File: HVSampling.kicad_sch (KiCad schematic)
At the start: 11 parts, among them K5 SPU01M-05, U13 TLV6002, U7 LM393, U8 4N35

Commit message: schematic: Assign all footprints
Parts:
- K5: footprint (none) -> yfs:DPU01M05
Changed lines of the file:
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@@
 			)
 		)
-		(property "Footprint" ""
+		(property "Footprint" "yfs:DPU01M05"
 			(at 177.8 35.56 0)
 			(effects

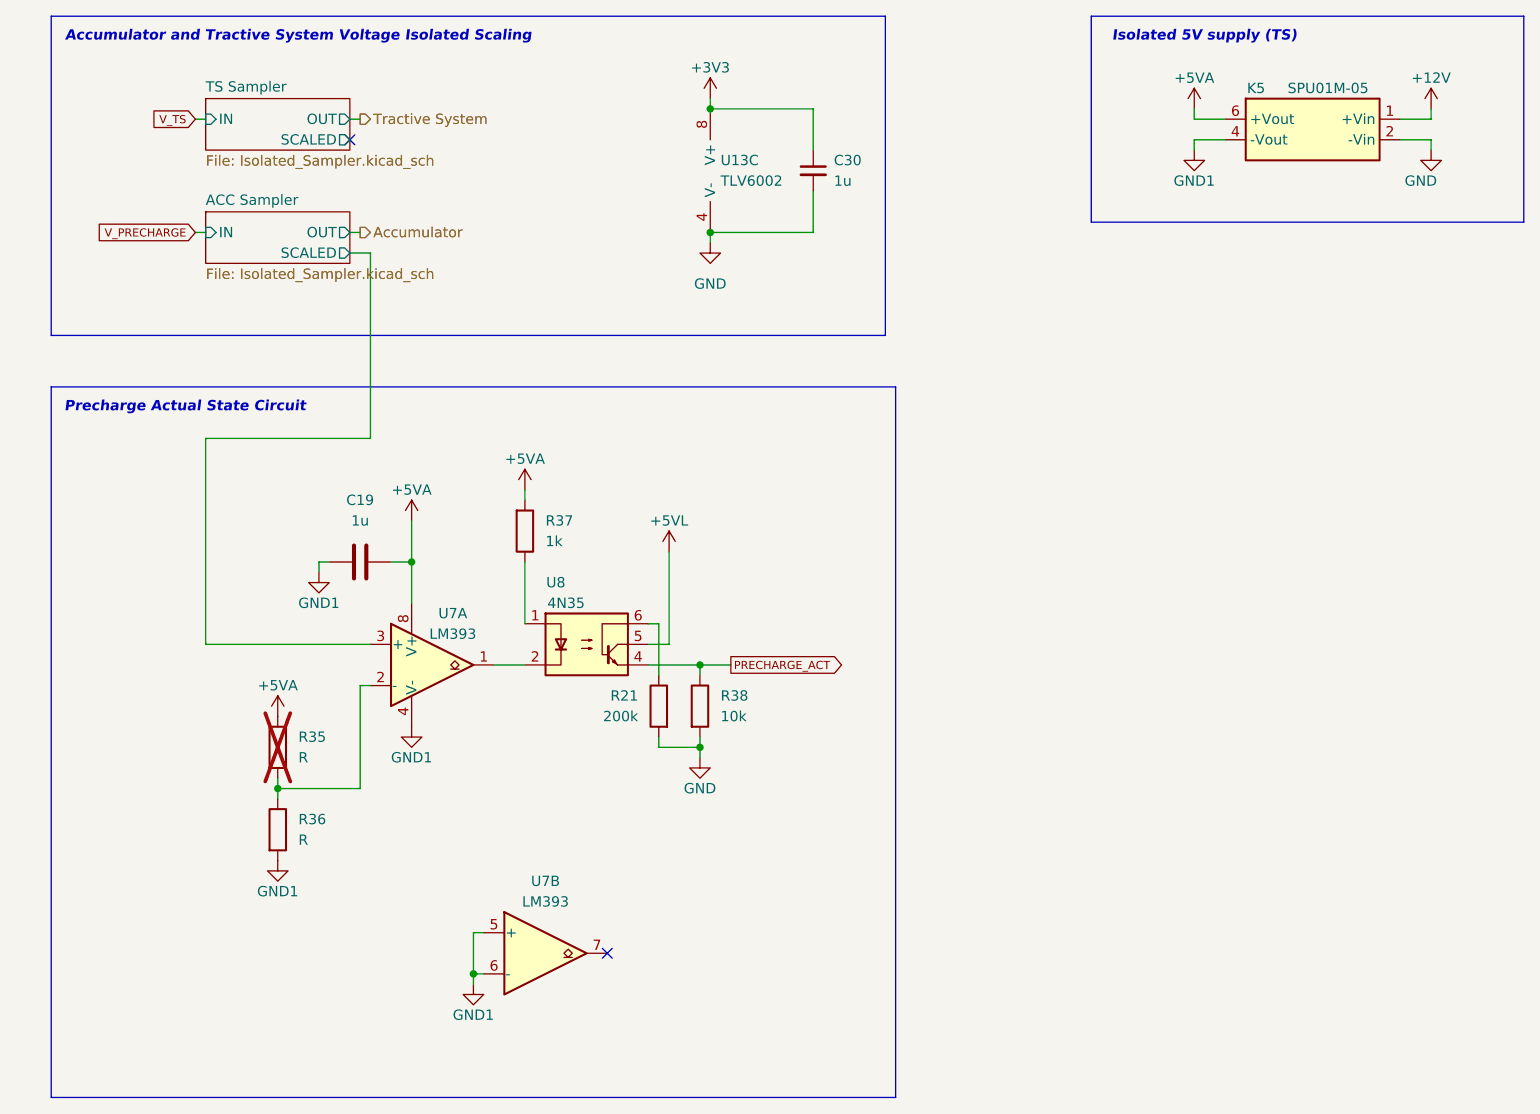
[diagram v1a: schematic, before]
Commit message: schematic: Reassign reference designators
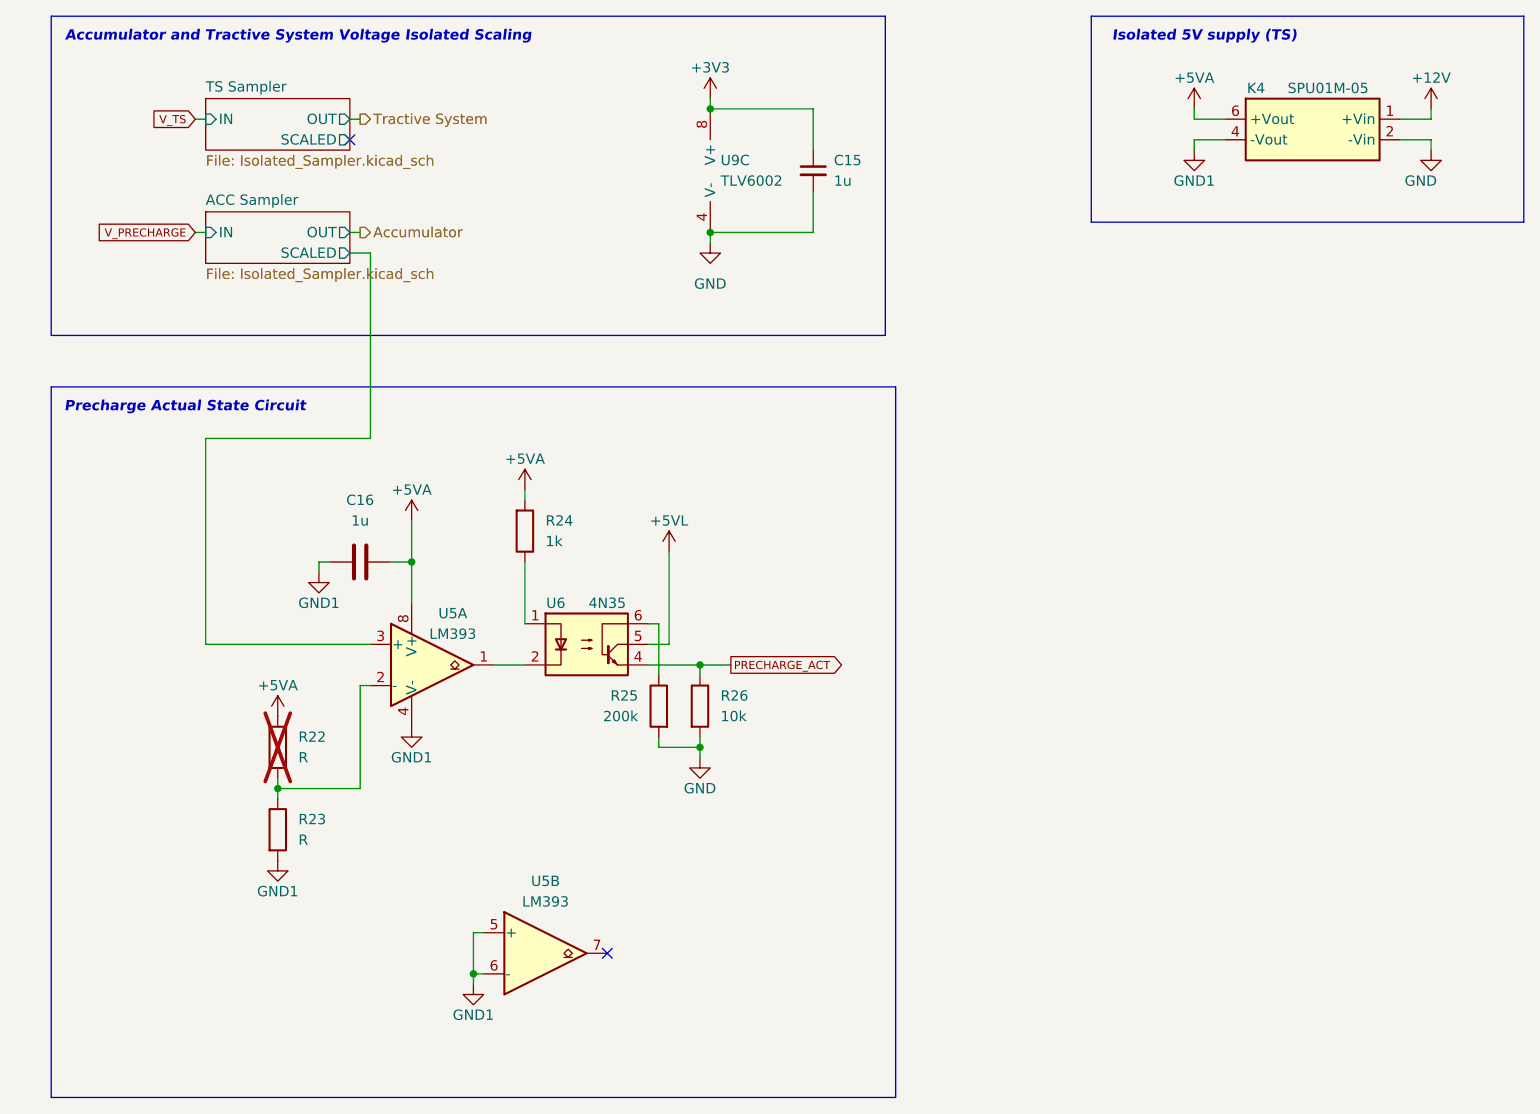
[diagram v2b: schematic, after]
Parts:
- renumbered C30 to C15, C19 to C16, K5 to K4, R35 to R22, R36 to R23, R37 to R24, R21 to R25, R38 to R26, U7 to U5, U8 to U6, U13 to U9
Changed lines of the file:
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@@
 		(on_board yes)
 		(dnp no)
-		(property "Reference" "K5"
+		(property "Reference" "K4"
 			(at 179.07 34.29 0)
 			(effects
@@
 			(project ""
 				(path "/c467677d-b98c-4488-bd11-965ef67263b2/5111e28e-8231-41c0-b506-a567affaf28a"
-					(reference "K5")
+					(reference "K4")
 					(unit 1)
 				)
@@
 		(on_board yes)
 		(dnp no)
-		(property "Reference" "U7"
+		(property "Reference" "U5"
 			(at 80.01 99.06 0)
 			(effects
@@
 			)
 		)
-		(property "Description" "Low-Power, Low-Offset Voltage, Dual Comparators, DIP-8/SOIC-8/TO-99-8"
+		(property "Description" ""
 			(at 77.47 105.41 0)
 			(effects
@@
 			(project "Precharge_PCB"
 				(path "/c467677d-b98c-4488-bd11-965ef67263b2/5111e28e-8231-41c0-b506-a567affaf28a"
-					(reference "U7")
+					(reference "U5")
 					(unit 1)
 				)
@@
 		(on_board yes)
 		(dnp no)
-		(fields_autoplaced yes)
-		(property "Reference" "U7"
+		(property "Reference" "U5"
 			(at 91.44 132.08 0)
 			(effects
@@
 			)
 		)
-		(property "Description" "Low-Power, Low-Offset Voltage, Dual Comparators, DIP-8/SOIC-8/TO-99-8"
+		(property "Description" ""
 			(at 91.44 140.97 0)
 			(effects
@@
 			(project "Precharge_PCB"
 				(path "/c467677d-b98c-4488-bd11-965ef67263b2/5111e28e-8231-41c0-b506-a567affaf28a"
-					(reference "U7")
+					(reference "U5")
 					(unit 2)
 				)
@@
 		(on_board yes)
 		(dnp no)
-		(property "Reference" "R21"
+		(property "Reference" "R25"
 			(at 102.87 109.22 0)
 			(effects
@@
 			(project "Precharge_PCB"
 				(path "/c467677d-b98c-4488-bd11-965ef67263b2/5111e28e-8231-41c0-b506-a567affaf28a"
-					(reference "R21")
+					(reference "R25")
 					(unit 1)
 				)
@@
 		(dnp no)
 		(fields_autoplaced yes)
-		(property "Reference" "C19"
+		(property "Reference" "C16"
 			(at 68.58 85.09 90)
 			(effects
@@
 			(project "Precharge_PCB"
 				(path "/c467677d-b98c-4488-bd11-965ef67263b2/5111e28e-8231-41c0-b506-a567affaf28a"
-					(reference "C19")
+					(reference "C16")
 					(unit 1)
 				)
@@
 		(dnp no)
 		(fields_autoplaced yes)
-		(property "Reference" "R36"
-			(at 60.96 124.46 0)
+		(property "Reference" "R23"
+			(at 60.96 124.4599 0)
 			(effects
 				(font
@@
 		)
 		(property "Value" "R"
-			(at 60.96 127 0)
+			(at 60.96 126.9999 0)
 			(effects
 				(font
@@
 			(project "Precharge_PCB"
 				(path "/c467677d-b98c-4488-bd11-965ef67263b2/5111e28e-8231-41c0-b506-a567affaf28a"
-					(reference "R36")
+					(reference "R23")
 					(unit 1)
 				)
@@
 		(dnp no)
 		(fields_autoplaced yes)
-		(property "Reference" "U7"
+		(property "Reference" "U5"
 			(at 76.2 104.14 0)
 			(effects
@@
 			(project "Precharge_PCB"
 				(path "/c467677d-b98c-4488-bd11-965ef67263b2/5111e28e-8231-41c0-b506-a567affaf28a"
-					(reference "U7")
+					(reference "U5")
 					(unit 3)
 				)
@@
 		(dnp no)
 		(fields_autoplaced yes)
-		(property "Reference" "U13"
+		(property "Reference" "U9"
 			(at 113.03 43.1799 0)
 			(effects
@@
 			(project "Precharge_PCB"
 				(path "/c467677d-b98c-4488-bd11-965ef67263b2/5111e28e-8231-41c0-b506-a567affaf28a"
-					(reference "U13")
+					(reference "U9")
 					(unit 3)
 				)
@@
 		(dnp no)
 		(fields_autoplaced yes)
-		(property "Reference" "R38"
-			(at 113.03 109.22 0)
+		(property "Reference" "R26"
+			(at 113.03 109.2199 0)
 			(effects
 				(font
@@
 		)
 		(property "Value" "10k"
-			(at 113.03 111.76 0)
+			(at 113.03 111.7599 0)
 			(effects
 				(font
@@
 			(project "Precharge_PCB"
 				(path "/c467677d-b98c-4488-bd11-965ef67263b2/5111e28e-8231-41c0-b506-a567affaf28a"
-					(reference "R38")
+					(reference "R26")
 					(unit 1)
 				)
@@
 		(dnp no)
 		(fields_autoplaced yes)
-		(property "Reference" "C30"
+		(property "Reference" "C15"
 			(at 127 43.1862 0)
 			(effects
@@
 			(project "Precharge_PCB"
 				(path "/c467677d-b98c-4488-bd11-965ef67263b2/5111e28e-8231-41c0-b506-a567affaf28a"
-					(reference "C30")
+					(reference "C15")
 					(unit 1)
 				)
@@
 		(on_board yes)
 		(dnp no)
-		(property "Reference" "U8"
-			(at 92.71 95.25 0)
+		(property "Reference" "U6"
+			(at 92.71 97.79 0)
 			(effects
 				(font
@@
 		)
 		(property "Value" "4N35"
-			(at 93.98 97.79 0)
+			(at 99.06 97.79 0)
 			(effects
 				(font
@@
 			(project "Precharge_PCB"
 				(path "/c467677d-b98c-4488-bd11-965ef67263b2/5111e28e-8231-41c0-b506-a567affaf28a"
-					(reference "U8")
+					(reference "U6")
 					(unit 1)
 				)
@@
 		(dnp yes)
 		(fields_autoplaced yes)
-		(property "Reference" "R35"
-			(at 60.96 114.3 0)
+		(property "Reference" "R22"
+			(at 60.96 114.2999 0)
 			(effects
 				(font
@@
 		)
 		(property "Value" "R"
-			(at 60.96 116.84 0)
+			(at 60.96 116.8399 0)
 			(effects
 				(font
@@
 			(project "Precharge_PCB"
 				(path "/c467677d-b98c-4488-bd11-965ef67263b2/5111e28e-8231-41c0-b506-a567affaf28a"
-					(reference "R35")
+					(reference "R22")
 					(unit 1)
 				)
@@
 		(on_board yes)
 		(dnp no)
-		(property "Reference" "R37"
+		(property "Reference" "R24"
 			(at 91.44 87.63 0)
 			(effects
@@
 			(project "Precharge_PCB"
 				(path "/c467677d-b98c-4488-bd11-965ef67263b2/5111e28e-8231-41c0-b506-a567affaf28a"
-					(reference "R37")
-					(unit 1)
-				)
+					(reference "R24")
+					(unit 1)
+				)

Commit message: schematic: Fill out most of the BOM
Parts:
- C16: Dist (none) -> LCSC; Dist # (none) -> C5199872; Mfr (none) -> Samsung; Mfr # (none) -> CL10B105KB8NQNC
- K4: Dist (none) -> Mouser; Dist # (none) -> 709-SPU01M-05; Mfr (none) -> MEAN WELL; Mfr # (none) -> SPU01M-05
- R24: Dist (none) -> LCSC; Dist # (none) -> C21190; Mfr (none) -> Uni-Royal; Mfr # (none) -> 0603WAF1001T5E
- R26: Dist (none) -> LCSC; Dist # (none) -> C25804; Mfr (none) -> Uni-Royal; Mfr # (none) -> 0603WAF1002T5E
- U5: Dist (none) -> LCSC; Dist # (none) -> C67470; Mfr (none) -> Texas Instruments; Mfr # (none) -> LM393DR
- U6: Dist (none) -> LCSC; Dist # (none) -> C4069; Mfr (none) -> onsemi; Mfr # (none) -> 4N35M
- U9: Dist (none) -> Mouser; Dist # (none) -> 595-TLV6002QDRQ1; Mfr (none) -> Texas Instruments; Mfr # (none) -> TLV6002QDRQ1

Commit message: pcb: Setup net classes and import components
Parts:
- K4: footprint yfs:DPU01M05 -> yfs:SPU01M-5
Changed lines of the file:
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@@
 	(title_block
 		(title "Precharge")
-		(date "2025-10-06")
+		(date "2025-12-13")
 		(rev "${REVISION}")
 		(company "York Formula Student")
@@
 			)
 		)
-		(property "Footprint" "yfs:DPU01M05"
+		(property "Footprint" "yfs:SPU01M-5"
 			(at 177.8 35.56 0)
 			(effects

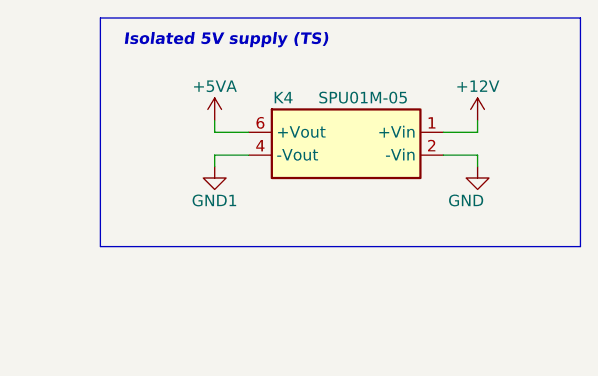
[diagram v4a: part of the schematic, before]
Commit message: Added TSAL power bypass jumper
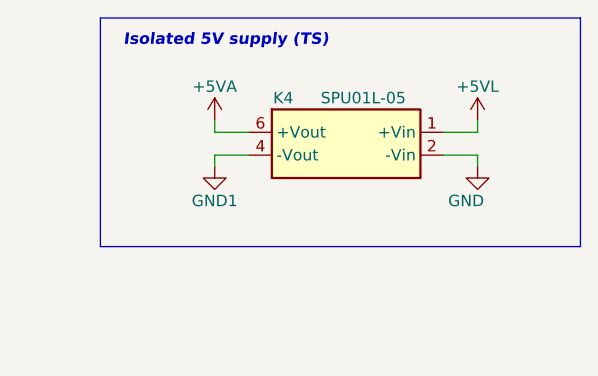
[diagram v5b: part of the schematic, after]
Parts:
- K4: value SPU01M-05 -> SPU01L-05
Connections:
- net +12V is gone; now on net +5VL: K4.1 (+Vin)
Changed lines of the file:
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@@
 			)
 		)
-		(property "Value" "SPU01M-05"
+		(property "Value" "SPU01L-05"
 			(at 187.96 34.29 0)
 			(effects
@@
 				(path "/c467677d-b98c-4488-bd11-965ef67263b2/5111e28e-8231-41c0-b506-a567affaf28a"
 					(reference "#PWR064")
+					(unit 1)
+				)
+			)
+		)
+	)
+	(symbol
+		(lib_id "power:+5VL")
+		(at 200.66 36.83 0)
+		(unit 1)
+		(exclude_from_sim no)
+		(in_bom yes)
+		(on_board yes)
+		(dnp no)
+		(property "Reference" "#PWR059"
+			(at 200.66 40.64 0)
+			(effects
+				(font
+					(size 1.27 1.27)
+				)
+				(hide yes)
+			)
+		)
+		(property "Value" "+5VL"
+			(at 200.66 33.02 0)
+			(effects
+				(font
+					(size 1.27 1.27)
+				)
+			)
+		)
+		(property "Footprint" ""
+			(at 200.66 36.83 0)
+			(effects
+				(font
+					(size 1.27 1.27)
+				)
+				(hide yes)
+			)
+		)
+		(property "Datasheet" ""
+			(at 200.66 36.83 0)
+			(effects
+				(font
+					(size 1.27 1.27)
+				)
+				(hide yes)
+			)
+		)
+		(property "Description" "Power symbol creates a global label with name \"+5VL\""
+			(at 200.66 36.83 0)
+			(effects
+				(font
+					(size 1.27 1.27)
+				)
+				(hide yes)
+			)
+		)
+		(pin "1"
+		)
+		(instances
+			(project "Precharge_PCB"
+				(path "/c467677d-b98c-4488-bd11-965ef67263b2/5111e28e-8231-41c0-b506-a567affaf28a"
+					(reference "#PWR059")
 					(unit 1)
 				)
@@
 					(unit 1)
 				)
-			)
-		)
-	)
-	(symbol
-		(lib_id "power:+12V")
-		(at 200.66 36.83 0)
-		(unit 1)
-		(exclude_from_sim no)
-		(in_bom yes)
-		(on_board yes)
-		(dnp no)
-		(property "Reference" "#PWR085"
-			(at 200.66 40.64 0)
-			(effects
-				(font
-					(size 1.27 1.27)
-				)
-				(hide yes)
-			)
-		)
-		(property "Value" "+12V"
-			(at 200.66 33.02 0)
-			(effects
-				(font
-					(size 1.27 1.27)
-				)
-			)
-		)
-		(property "Footprint" ""
-			(at 200.66 36.83 0)
-			(effects
-				(font
-					(size 1.27 1.27)
-				)
-				(hide yes)
-			)
-		)
-		(property "Datasheet" ""
-			(at 200.66 36.83 0)
-			(effects
-				(font
-					(size 1.27 1.27)
-				)
-				(hide yes)
-			)
-		)
-		(property "Description" "Power symbol creates a global label with name \"+12V\""
-			(at 200.66 36.83 0)
-			(effects
-				(font
-					(size 1.27 1.27)
-				)
-				(hide yes)
-			)
-		)
-		(pin "1"
-		)
-		(instances
-			(project "Precharge_PCB"
-				(path "/c467677d-b98c-4488-bd11-965ef67263b2/5111e28e-8231-41c0-b506-a567affaf28a"
-					(reference "#PWR085")
-					(unit 1)
-				)

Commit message: schematic: Fix BOM for SPU01L-05 DC-DC converter
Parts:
- K4: Dist Mouser -> DigiKey; Dist # 709-SPU01M-05 -> 1866-4835-ND; Mfr # SPU01M-05 -> SPU01L-05
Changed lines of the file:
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@@
 			)
 		)
-		(property "Dist" "Mouser"
+		(property "Dist" "DigiKey"
 			(at 177.8 35.56 0)
 			(effects
@@
 			)
 		)
-		(property "Dist #" "709-SPU01M-05"
+		(property "Dist #" "1866-4835-ND"
 			(at 177.8 35.56 0)
 			(effects
@@
 			)
 		)
-		(property "Mfr #" "SPU01M-05"
+		(property "Mfr #" "SPU01L-05"
 			(at 177.8 35.56 0)
 			(effects
